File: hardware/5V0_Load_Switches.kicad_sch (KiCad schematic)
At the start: 28 parts, among them Q18 SI2302DDS-T1-GE3, Q19 SI2302DDS-T1-GE3, Q20 SI2302DDS-T1-GE3, U1 LMV321RIYLT, U10 INA199C3DCKR, U4 INA199C1DCKR, U5 NVTFS5116PLTAG, U6 NVTFS5116PLTAG, U7 NVTFS5116PLTAG, U9 INA199C3DCKR

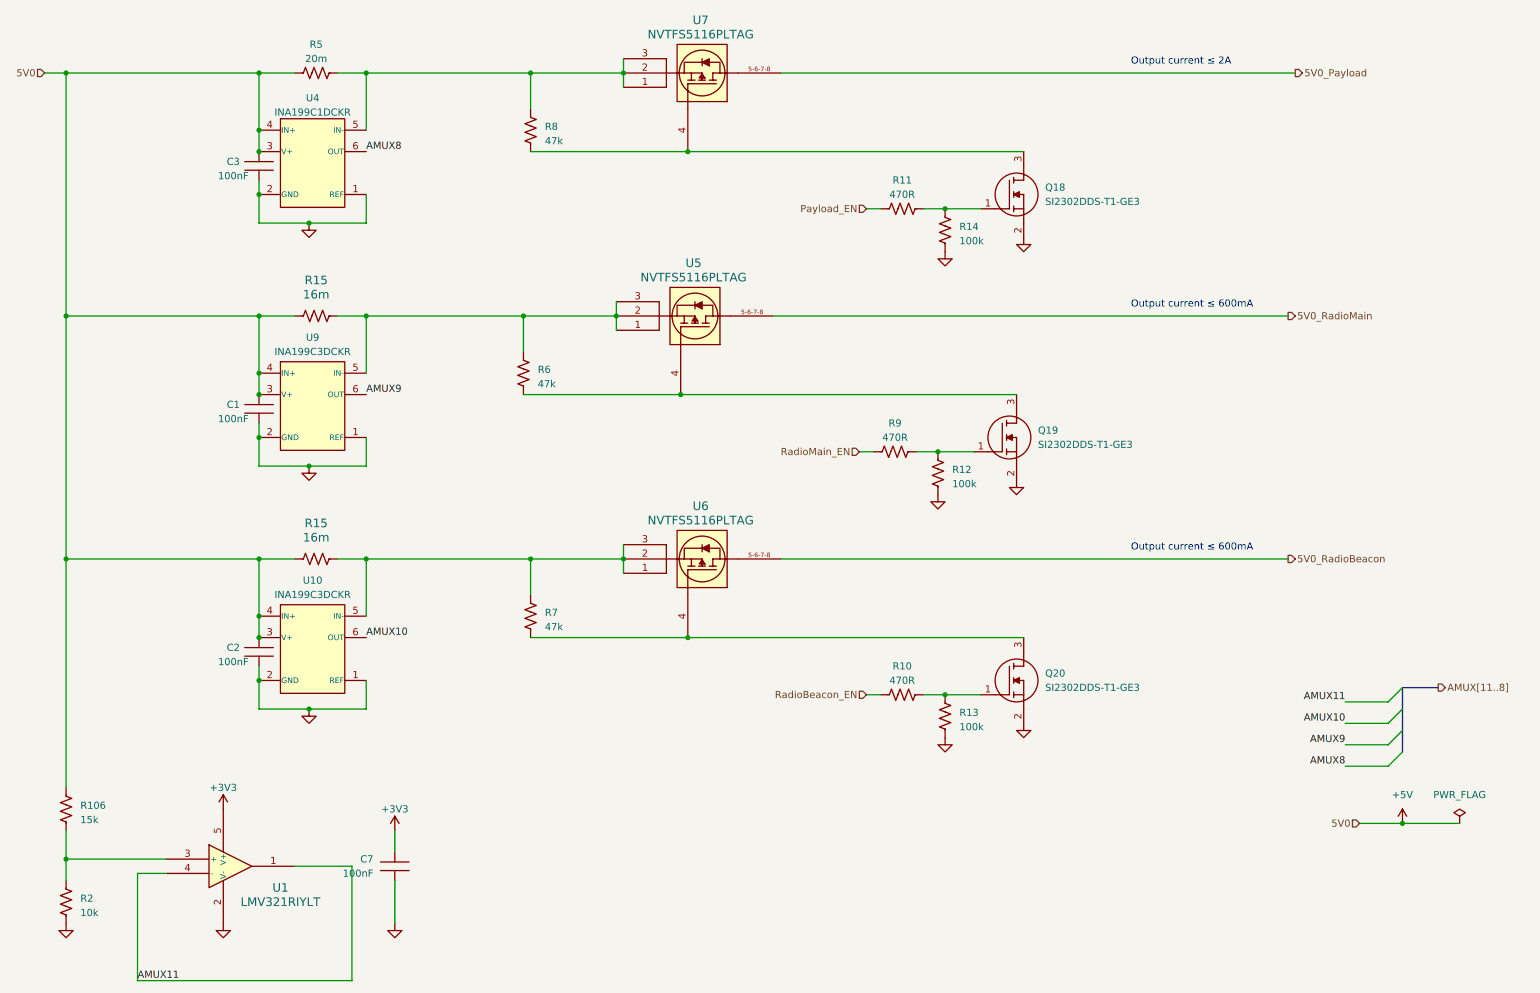
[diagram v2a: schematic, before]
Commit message: hardware: Updating the schematic and layout to solve #8, #9 and #10.
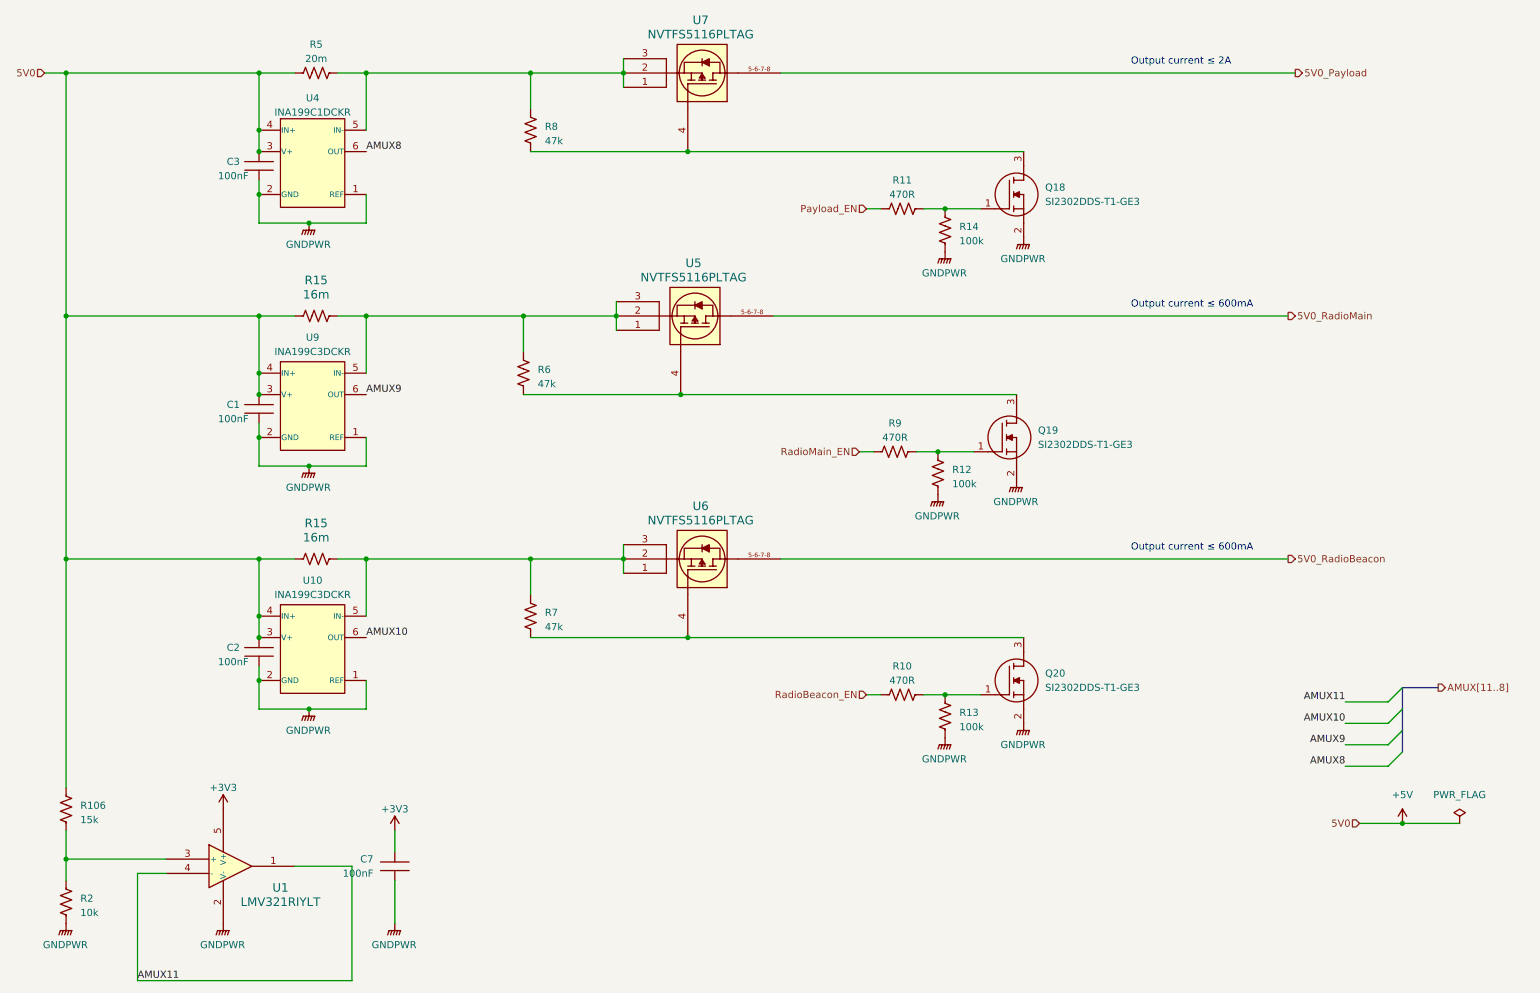
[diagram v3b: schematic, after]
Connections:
- net GND renamed GNDPWR

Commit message: hardware: Updating the MPPT circuit.
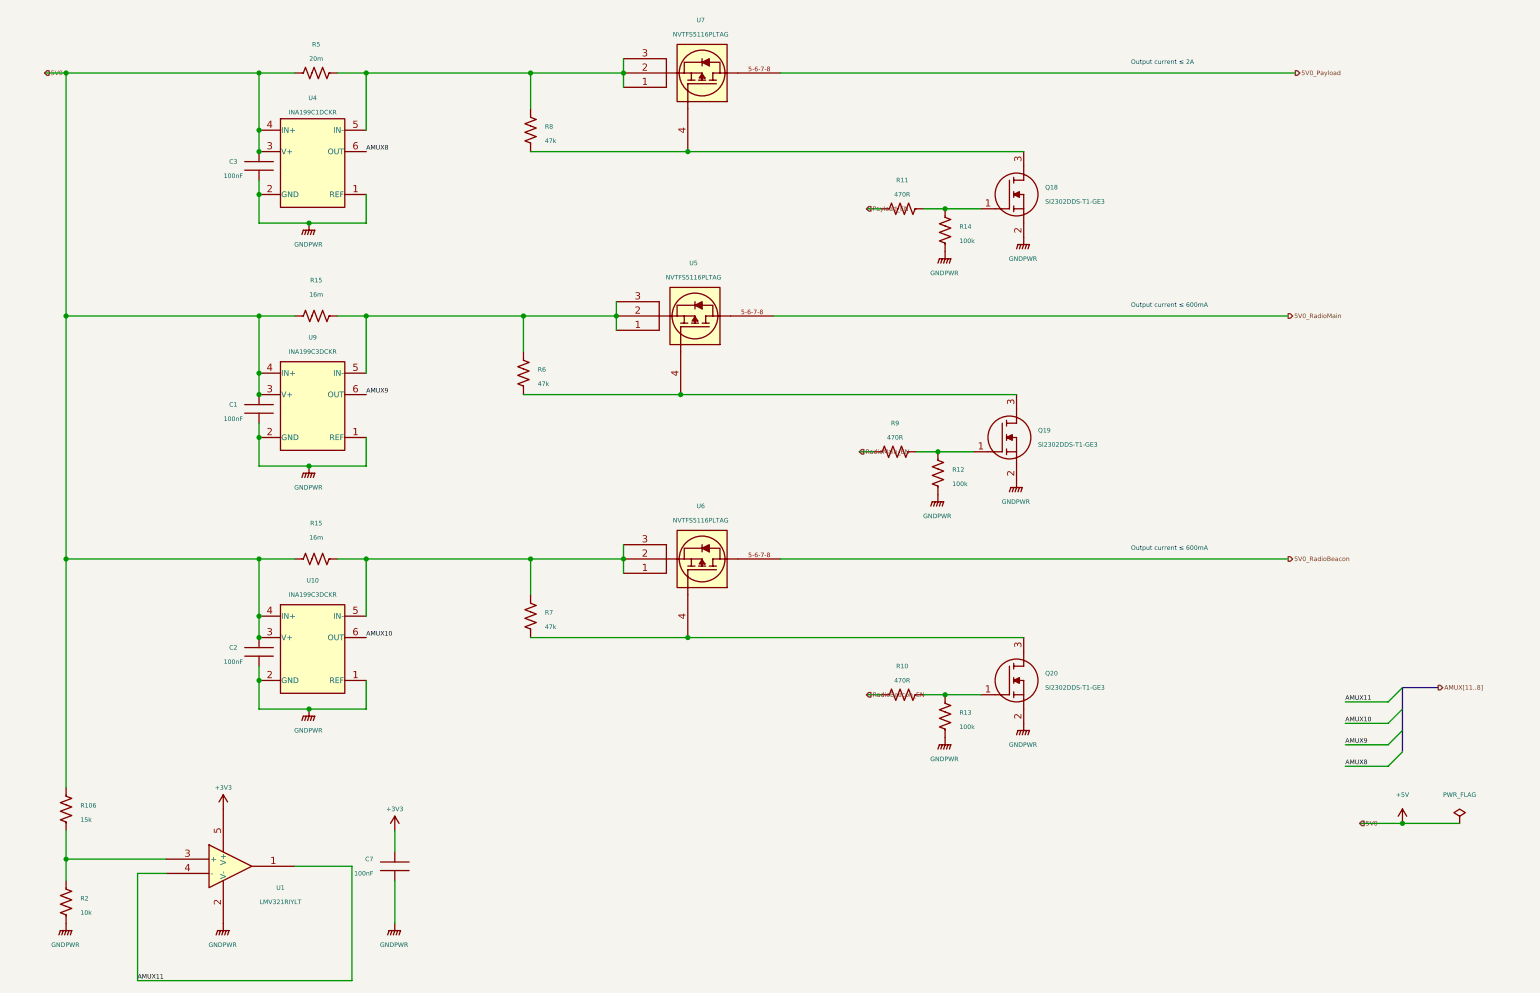
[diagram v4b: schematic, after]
